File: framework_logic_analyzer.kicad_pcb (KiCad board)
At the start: 4 copper layers, 54 x 50 mm, 148 parts, among them IC1 TXU0104QWBQARQ1, IC2 TXU0104QWBQARQ1, IC3 TXU0104QWBQARQ1, IC4 TXU0104QWBQARQ1, IC5 CYUSB3014-BZXC, IC6 XC9285B18CMR-G, J1 10152803-00011LF, J3 Conn_ARM_JTAG_SWD_10, J4 6101XX249121_610108249121, J5 6101XX249121_610108249121, J6 6101XX249121_610108249121, J7 6101XX249121_610108249121, Q1 MMBT3904, Q2 MMBT3904, Q3 MMBT3904, U1 NCP360SNT1G, U2 TUSB321RWBR, U4 SC189CSKTRT, U5 M24M02-DR, U7 TUSB542RWQR, Y1 19.200 MHz

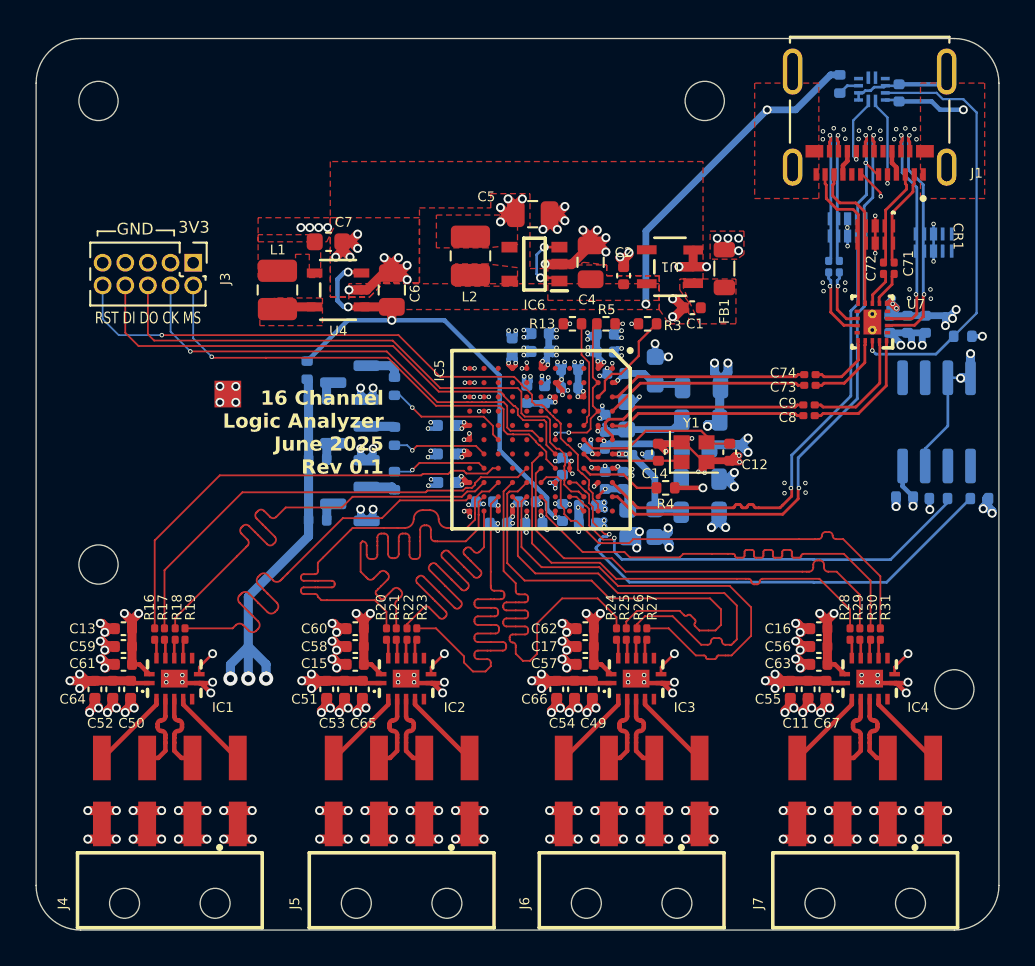
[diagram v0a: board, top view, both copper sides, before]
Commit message: implement all SML review nits
hopefully
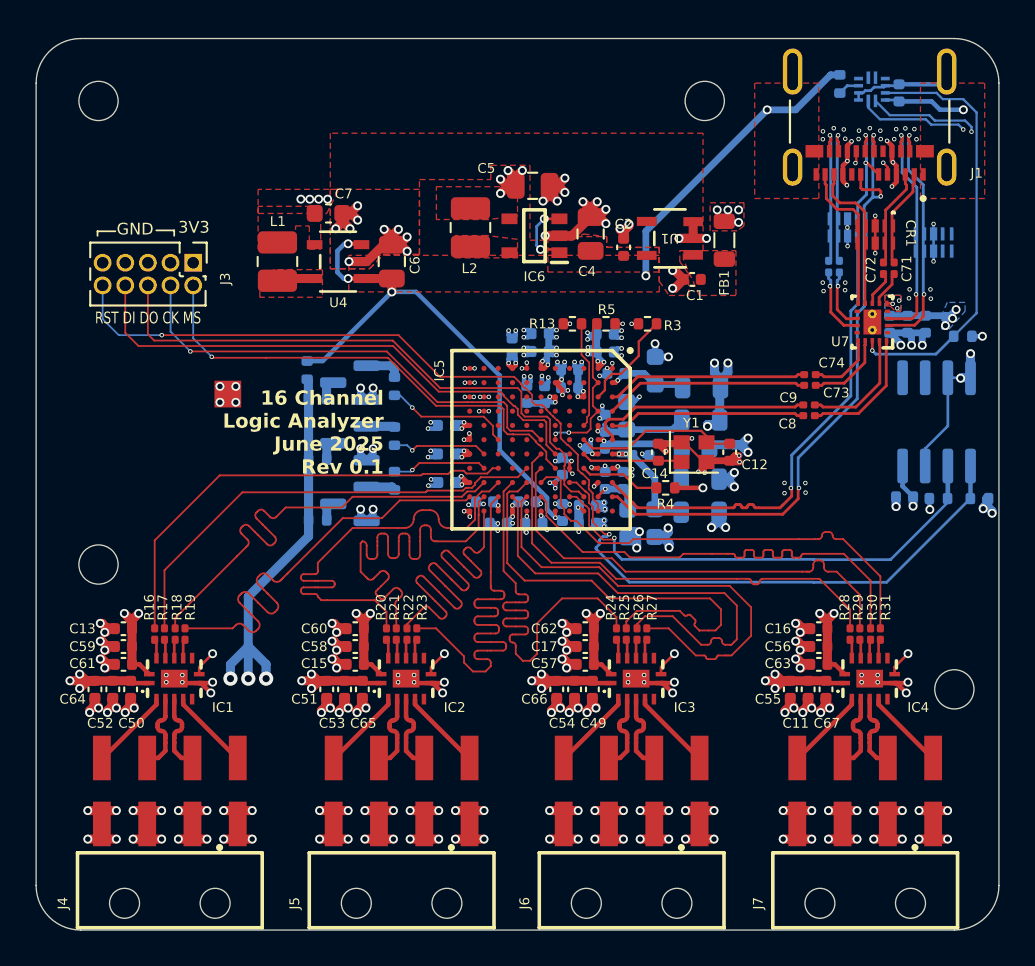
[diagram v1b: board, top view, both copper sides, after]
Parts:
- C69, C70, C71, C72, C73, C74, C8, C9: footprint Capacitor_SMD:C_0201_0603Metric -> logic_analyzer:C_0201_0603Metric_USB
- R16, R17, R18, R19, R20, R21, R22, R23, R24, R25, R26, R27, R28, R29, R30, R31: value 50R 1% -> 60R 1%; footprint Resistor_SMD:R_0201_0603Metric -> logic_analyzer:R_0201_0603Metric_input
- moved C1 1.59 mm to (146.2, 69.6)
- moved C2 1.59 mm to (142.3, 67.8)
- moved C4 1.59 mm to (140.5, 67.1)
- moved C5 1.59 mm to (137.2, 64.4)
- moved C6 1.59 mm to (129.3, 68.6)
- moved C7 1.59 mm to (125.8, 65.9)
- moved FB1 1.59 mm to (148.0, 67.4)
- moved IC6 1.59 mm to (137.3, 67.2)
- moved L1 1.59 mm to (122.9, 68.6)
- moved L2 1.59 mm to (133.8, 66.7)
- moved U1 1.59 mm to (144.9, 67.3)
- moved U4 1.59 mm to (126.3, 68.6)
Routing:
- net /USB-C/VBUS_CON_IN: track 2.81 -> 13.4 mm, vias 4 -> 10
- net /USB-C/CC2: track 4.16 -> 13.7 mm, vias 1 -> 2
- net /USB-C/CC1: track 5.41 -> 12.7 mm, vias 1 -> 2
- net +1V8: track 66.5 -> 63.4 mm, vias 52 -> 53
- net /I2C_SDA: track 25.3 -> 27.1 mm
- net /I2C_SCL: track 29.2 -> 31.0 mm
- net /USB-C/SSD-: track 36.1 -> 37.1 mm
- added copper zone on B.Cu, net +1V8
- added copper zone on In3.Cu, net /USB-C/VBUS_CON_IN
- added copper zone on In4.Cu, net GND
- removed copper zone on In2.Cu, net GND
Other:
- copper layers 4 -> 6

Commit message: ground plane to the max!
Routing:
- added copper zone on In3.Cu, net GND
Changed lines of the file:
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@@
 		(net_name "GND")
 		(locked yes)
-		(layers "In1.Cu" "In4.Cu")
+		(layers "In1.Cu" "In3.Cu" "In4.Cu")
 		(name "GND")
 		(hatch edge 0.5)

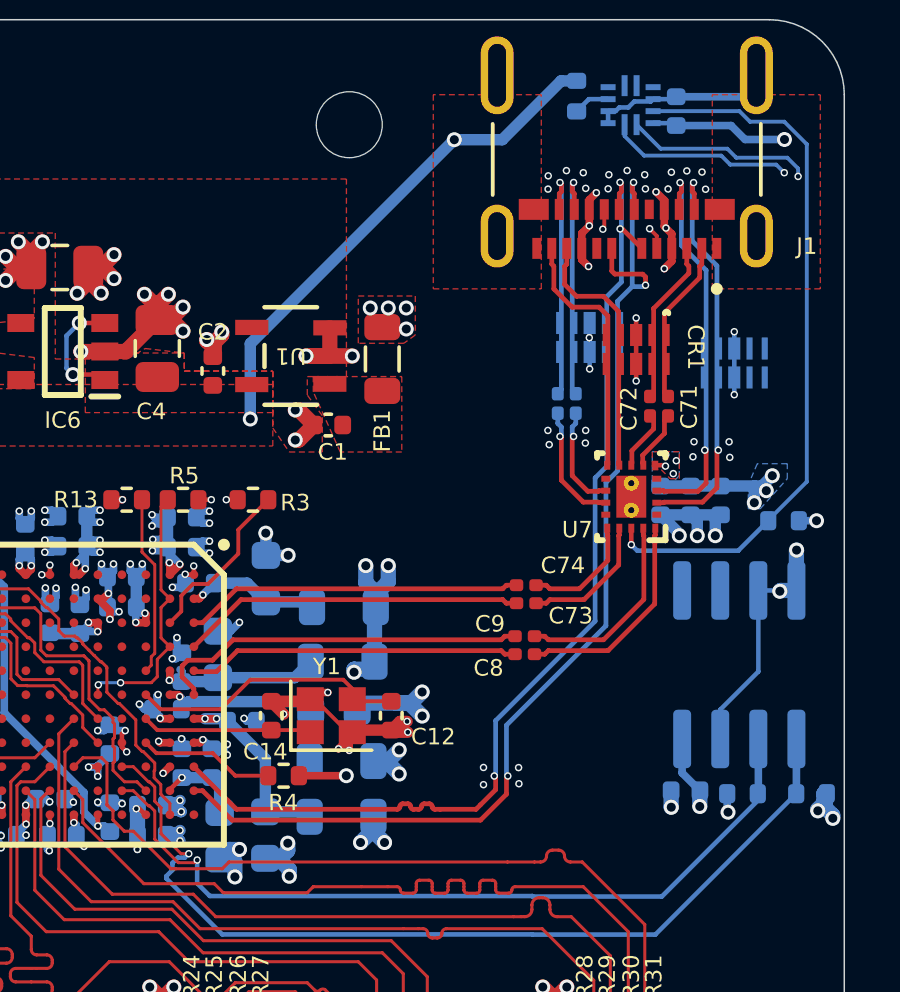
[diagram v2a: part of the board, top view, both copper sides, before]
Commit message: length matching on usb
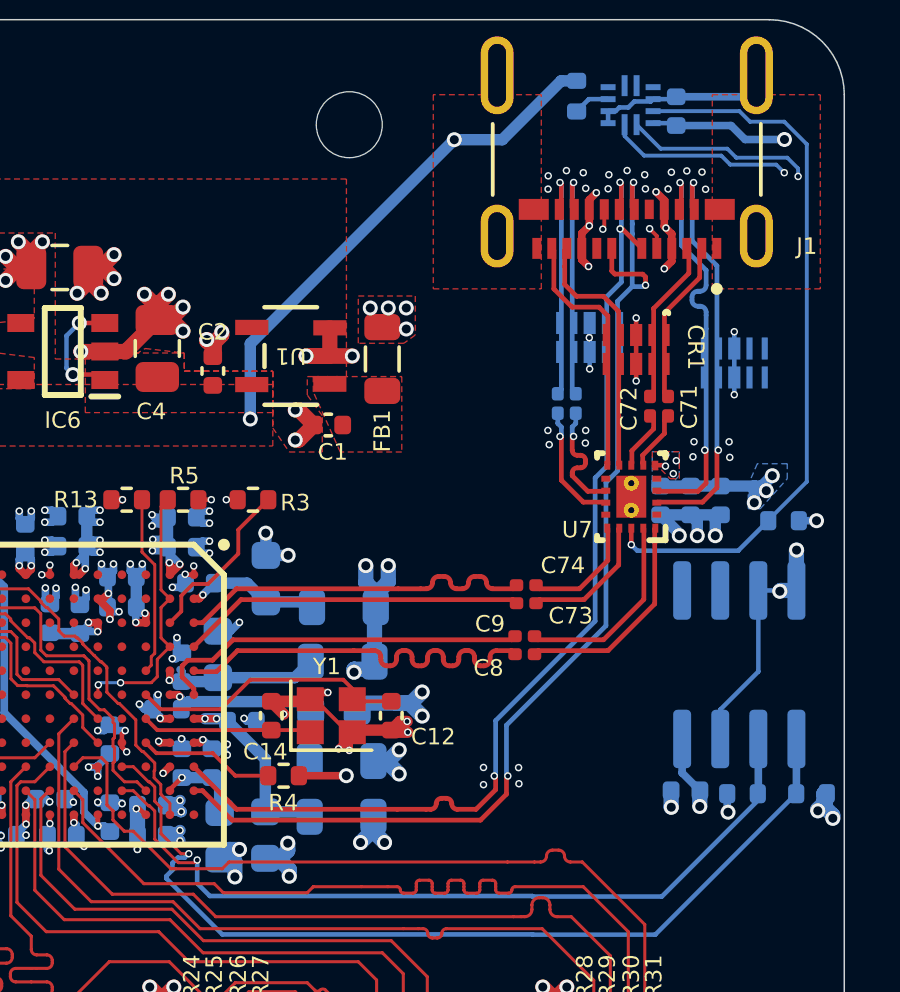
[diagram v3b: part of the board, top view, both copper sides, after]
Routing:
- net /USB-C/SS_TX+: track 11.1 -> 13.6 mm
- net /USB-C/SS_RX-: track 11.3 -> 12.1 mm
- net /USB-C/SS_REDRIVE_TX2-: track 3.52 -> 4.09 mm
- net /USB-C/SS_RX1-: track 13.1 -> 13.7 mm
